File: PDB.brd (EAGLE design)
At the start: 130.3 x 166.9 mm, 55 parts, among them J1 B06B-HCMKK, J2 B06B-HCMKK, J3 SS-6488-NF-A431, J4 SS-6488-NF-A431, J5 B06B-HCMKK, J6 B03B-HCMKS, J7 B03B-HCMKS, J8 SS-6488-NF-A431

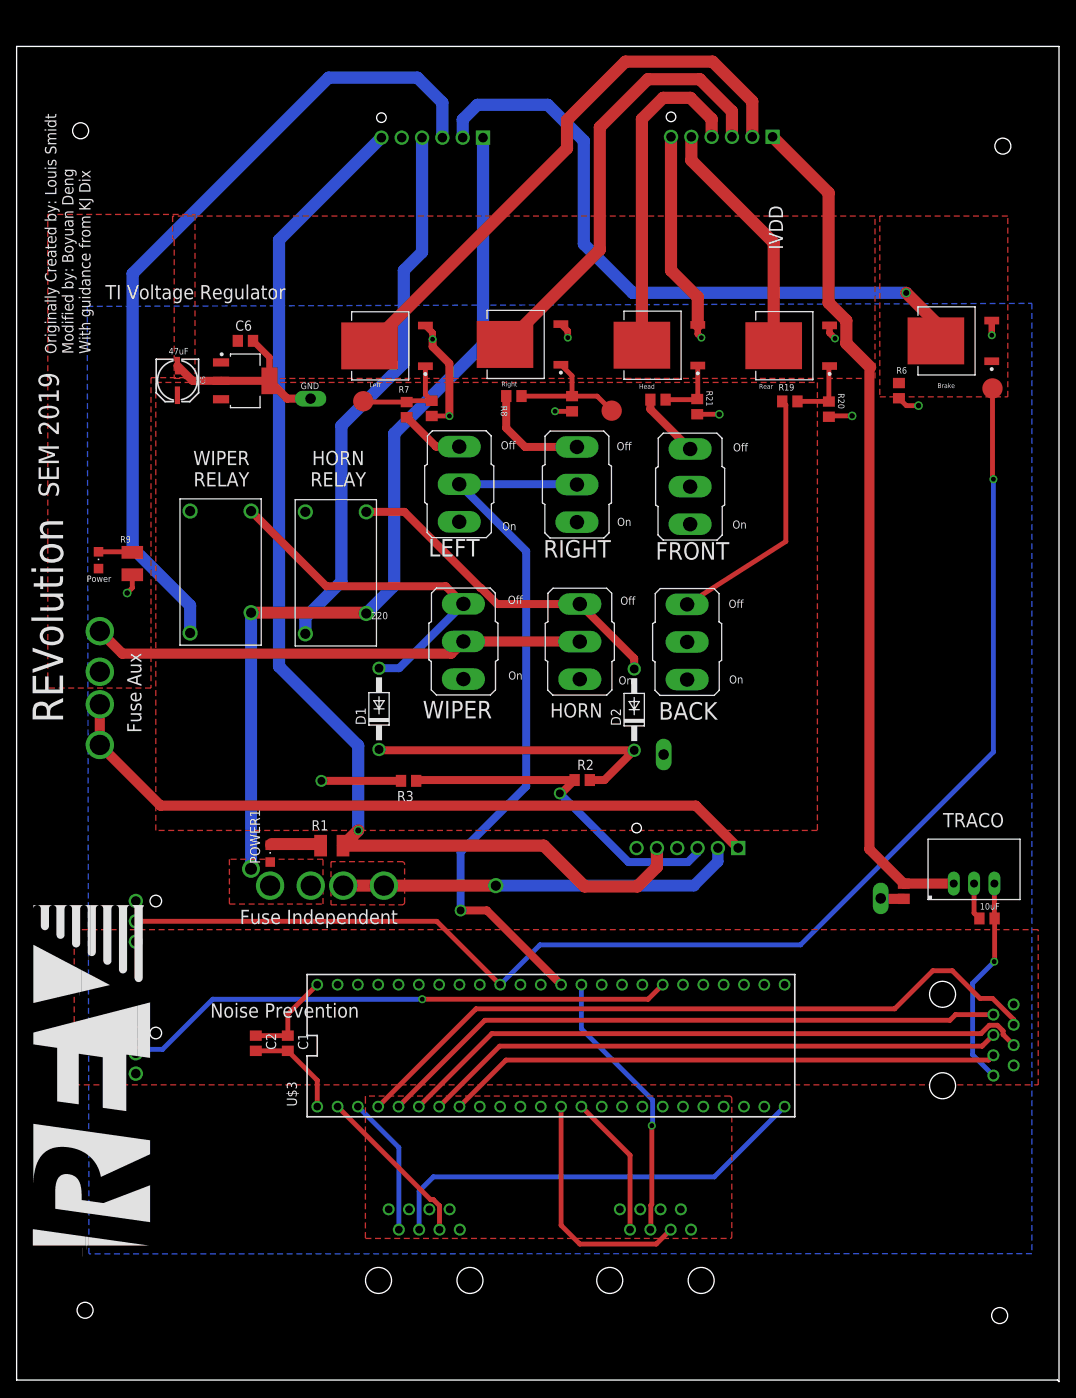
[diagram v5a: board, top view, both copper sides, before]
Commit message: Edited skilscreen to fit new connector arrangement, reversed ethernet cable to screen to correct direction.
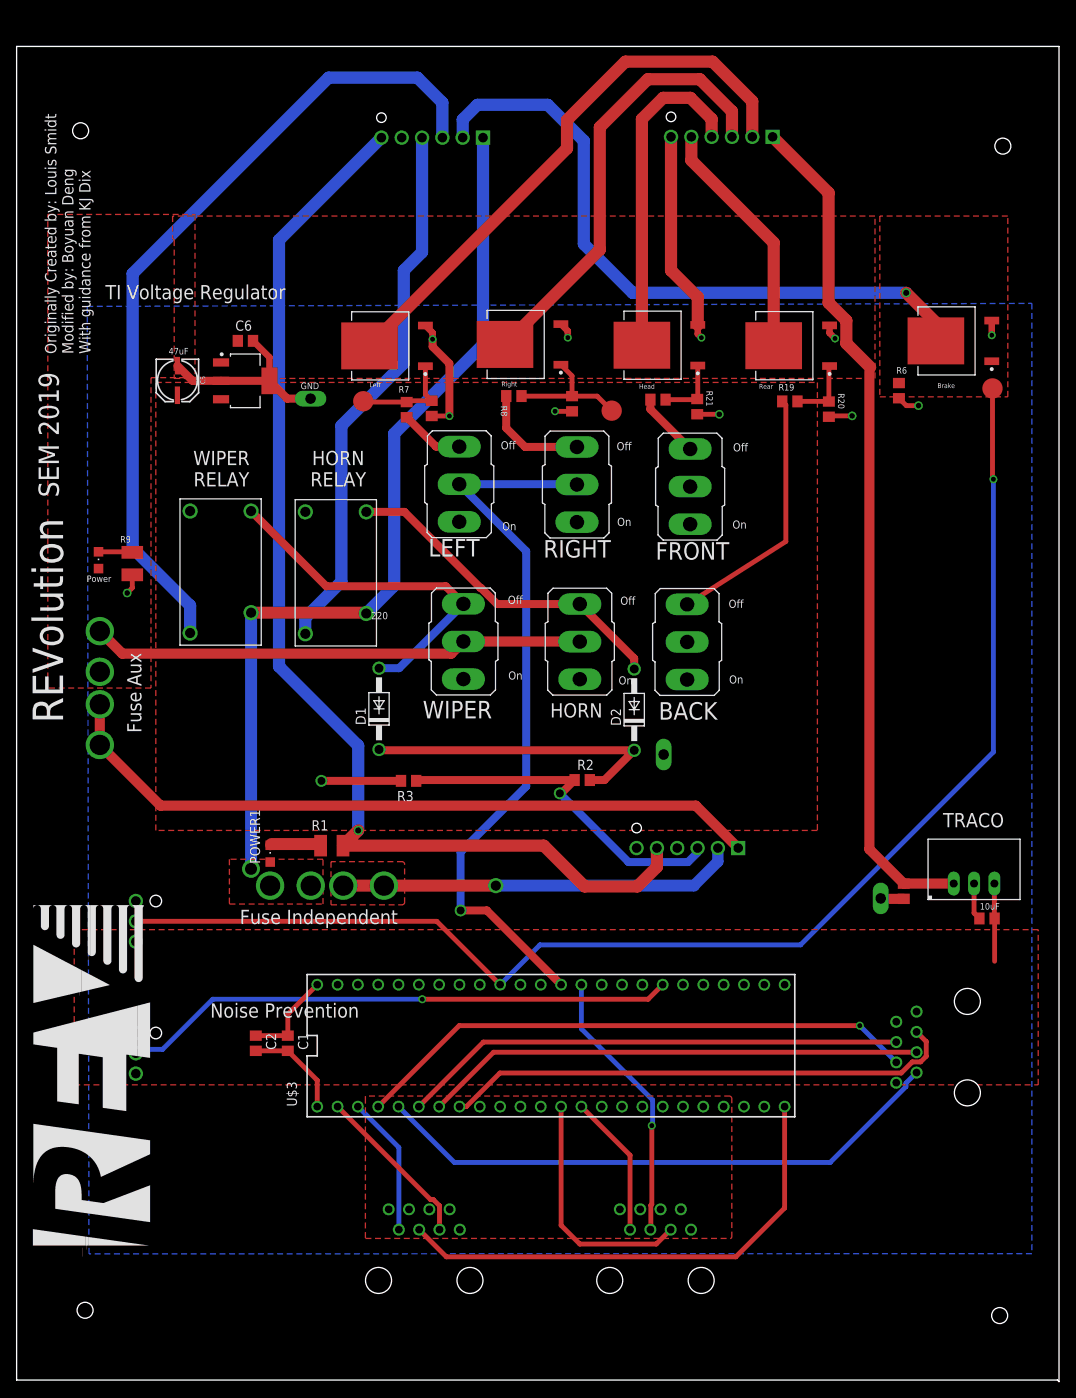
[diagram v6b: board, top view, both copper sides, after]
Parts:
- moved J8 12.5 mm to (114.4, 34.0), turned to 270 degrees
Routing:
- net CLK_SW: track 89.7 -> 70.9 mm, vias 0 -> 1
- net CS: track 79.9 -> 63.0 mm
- net 5V_REG: track 38.1 -> 21.6 mm, vias 1 -> 0
- net DC: track 73.0 -> 62.5 mm
- net CLK_A: track 54.9 -> 62.3 mm
- net MOSI_SW: track 79.1 -> 72.6 mm
- net RESET: track 69.4 -> 64.5 mm

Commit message: Code folder added.
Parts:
- R2, R3: value 4K -> 4.7K
- R20: value 4.7K -> 47K
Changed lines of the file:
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@@
 <attribute name="VALUE" x="96.4576" y="109.6684" size="1.27" layer="27" rot="SR0"/>
 </element>
-<element name="R20" library="rcl" library_urn="urn:adsk.eagle:library:334" package="R0805" package3d_urn="urn:adsk.eagle:package:23553/2" value="4.7K" x="103.435" y="109.262" smashed="yes" rot="R90">
+<element name="R20" library="rcl" library_urn="urn:adsk.eagle:library:334" package="R0805" package3d_urn="urn:adsk.eagle:package:23553/2" value="47K" x="103.435" y="109.262" smashed="yes" rot="R90">
 <attribute name="NAME" x="104.5704" y="111.2604" size="0.8128" layer="25" rot="SR270"/>
 <attribute name="POPULARITY" value="85" x="103.435" y="109.262" size="1.778" layer="27" rot="R90" display="off"/>
@@
 <attribute name="VALUE" x="81.894" y="69.668" size="1.27" layer="27" ratio="10" rot="R90"/>
 </element>
-<element name="R2" library="master_library" package="R0805" package3d_urn="urn:adsk.eagle:package:2274104/1" value="4K" x="72.6" y="62.9" smashed="yes">
+<element name="R2" library="master_library" package="R0805" package3d_urn="urn:adsk.eagle:package:2274104/1" value="4.7K" x="72.6" y="62.9" smashed="yes">
 <attribute name="NAME" x="71.965" y="64.17" size="1.27" layer="25"/>
 <attribute name="VALUE" x="71.965" y="60.36" size="1.27" layer="27"/>
 </element>
-<element name="R3" library="master_library" package="R0805" package3d_urn="urn:adsk.eagle:package:2274104/1" value="4K" x="50.9" y="62.8" smashed="yes" rot="R180">
+<element name="R3" library="master_library" package="R0805" package3d_urn="urn:adsk.eagle:package:2274104/1" value="4.7K" x="50.9" y="62.8" smashed="yes" rot="R180">
 <attribute name="NAME" x="51.535" y="61.53" size="1.27" layer="25" rot="R180"/>
 <attribute name="VALUE" x="51.535" y="65.34" size="1.27" layer="27" rot="R180"/>
